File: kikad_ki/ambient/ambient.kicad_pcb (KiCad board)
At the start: 2 copper layers, 80 x 66 mm, 69 parts, among them J1 5V DC, J2 FPC 01x10 Female, J3 LED Array, Q1 2N3904, SW1 Reset, SW2 Next, SW3 Select, SW4 Modify, U1 ATmega328P-PU, U2 AT24C256, U3 AT24C256, U4 AT24C256, U5 AT24C256, Y1 16 MHz

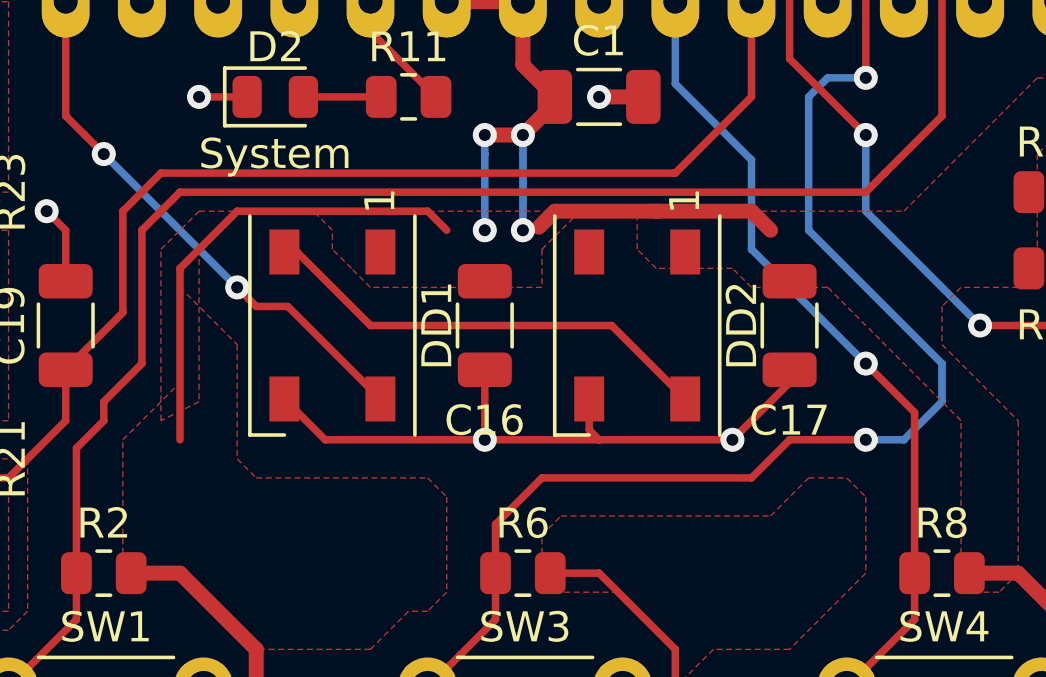
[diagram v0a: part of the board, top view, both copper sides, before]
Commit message: RGB WS2812B -> RGBWW SK6812
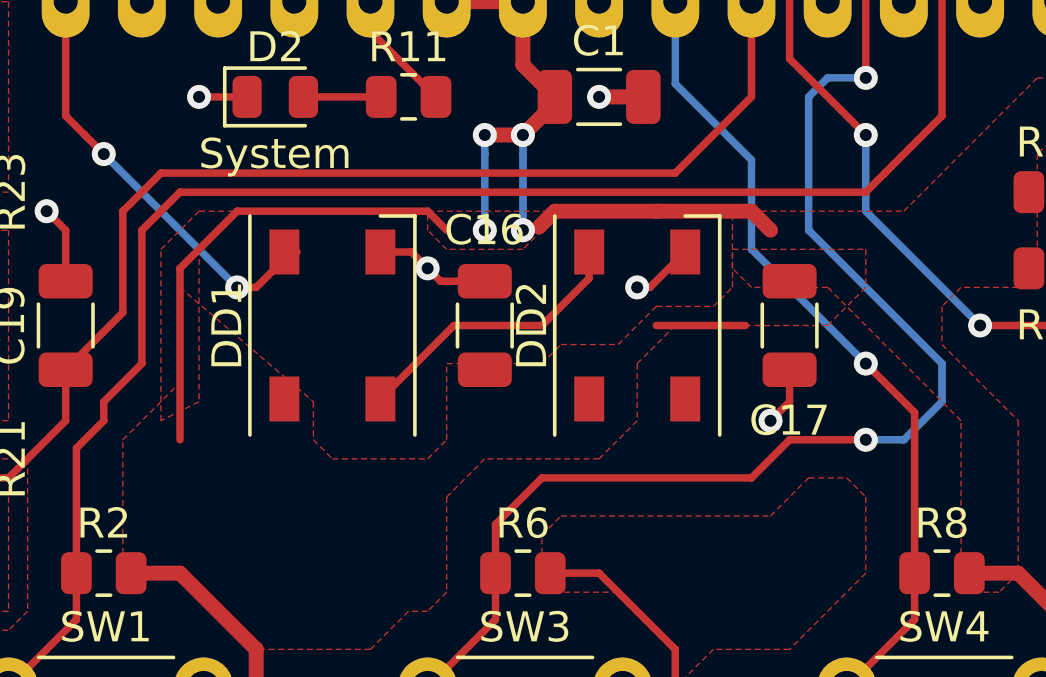
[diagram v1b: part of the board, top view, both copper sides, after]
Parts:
- DD1, DD2: value WS2812B -> SK6812; footprint LED_SMD:LED_WS2812B_PLCC4_5.0x5.0mm_P3.2mm -> LED_SMD:LED_SK6812_PLCC4_5.0x5.0mm_P3.2mm
- turned C16 to 90 degrees
- turned DD1 to 90 degrees
- turned DD2 to 90 degrees
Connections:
- DD1 pad 1: VCC -> GND
- DD1 pad 2: Net-(DD1-Pad2) -> PREVIEW_ARRAY
- DD1 pad 3: GND -> VCC
- DD1 pad 4: PREVIEW_ARRAY -> Net-(DD1-Pad4)
- DD2 pad 1: VCC -> GND
- DD2 pad 2: Net-(DD2-Pad2) -> Net-(DD1-Pad4)
- DD2 pad 3: GND -> VCC
- DD2 pad 4: Net-(DD1-Pad2) -> Net-(DD2-Pad4)
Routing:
- net Net-(DD1-Pad2): track 15.6 -> 0.00 mm
- net GND: track 64.6 -> 50.7 mm, vias 78 -> 79
- net Net-(DD1-Pad4): track 0.00 -> 9.18 mm
- net PREVIEW_ARRAY: track 18.3 -> 14.6 mm
- net VCC: track 165.5 -> 168.5 mm

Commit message: gerber files
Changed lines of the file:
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@@
       (effects (font (size 0.8 0.8) (thickness 0.12)))
     )
-    (pad 1 smd roundrect (at -1.4625 0 90) (size 1.125 1.75) (layers F.Cu F.Paste F.Mask) (roundrect_rratio 0.2222204444444444)
+    (pad 1 smd roundrect (at -1.4625 0 90) (size 1.125 1.75) (layers F.Cu F.Paste F.Mask) (roundrect_rratio 0.2222195555555556)
       (net 2 GND))
-    (pad 2 smd roundrect (at 1.4625 0 90) (size 1.125 1.75) (layers F.Cu F.Paste F.Mask) (roundrect_rratio 0.2222204444444444)
+    (pad 2 smd roundrect (at 1.4625 0 90) (size 1.125 1.75) (layers F.Cu F.Paste F.Mask) (roundrect_rratio 0.2222195555555556)
       (net 37 ARRAY_DIN))
     (model ${KISYS3DMOD}/Resistor_SMD.3dshapes/R_1206_3216Metric.wrl
@@
     (polygon
       (pts
-        (xy 93.98 80.01) (xy 52.07 80.01) (xy 50.165 78.105) (xy 57.15 78.105) (xy 64.135 78.105)
-        (xy 66.675 78.105) (xy 90.17 78.105) (xy 92.075 76.2) (xy 92.075 67.945) (xy 91.44 67.31)
-        (xy 91.44 66.675) (xy 93.98 64.135)
-      )
-    )
+        (xy 93.98 80.01) (xy 52.07 80.01) (xy 50.165 78.105) (xy 57.15 78.105) (xy 61.595 78.105)
+        (xy 64.135 75.565) (xy 66.675 78.105) (xy 90.17 78.105) (xy 92.075 76.2) (xy 92.075 67.945)
+        (xy 91.44 67.31) (xy 91.44 66.675) (xy 93.98 64.135)
+      )
+    )

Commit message: updated design + pcb
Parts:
- removed  : MountingHole_3.2mm_M3, MountingHole:MountingHole_3.2mm_M3 (x3)
- removed the C13 at (86.4, 28.6)
- removed C14, C15, C16, C17, C19: 0.1u, Capacitor_SMD:C_1206_3216Metric
- removed the C3 at (59.4, 26.7)
- removed D4, D5: 1N4735A, Diode_THT:D_DO-41_SOD81_P10.16mm_Horizontal
- removed DD1, DD2: SK6812, LED_SMD:LED_SK6812_PLCC4_5.0x5.0mm_P3.2mm
- removed R14, R15, R16, R17: 4.7k, Resistor_SMD:R_0805_2012Metric
- removed R22, R23: 0.02, Resistor_SMD:R_2512_6332Metric
- removed R9: 68, Resistor_SMD:R_0805_2012Metric
- removed the SW1 at (41.9, 69.2)
- removed SW4: Modify, Button_Switch_THT:SW_PUSH_6mm
- removed U3, U4, U5: AT24C256, Package_DIP:DIP-8_W7.62mm_LongPads
- added ?: , rasp:prv_small, B.Cu at (17.2, 14.8)
- added C6: 22, Capacitor_SMD:C_0805_2012Metric, F.Cu at (51.1, 9.91)
- added H1: MountingHole, MountingHole:MountingHole_3.2mm_M3_DIN965_Pad, F.Cu at (3.56, 13.2)
- added H2: MountingHole, MountingHole:MountingHole_3.2mm_M3_DIN965_Pad, F.Cu at (32.0, 32.3)
- added H3: MountingHole, MountingHole:MountingHole_3.2mm_M3_DIN965_Pad, F.Cu at (76.2, 3.81)
- added H4: MountingHole, MountingHole:MountingHole_3.2mm_M3_DIN965_Pad, F.Cu at (77.4, 32.5)
- added LED1: Blue LED, LED_THT:LED_D3.0mm_Clear, F.Cu at (86.3, 27.8)
- added LED2: Green LED, LED_THT:LED_D3.0mm_Clear, F.Cu at (83.8, 33.4)
- C1: renamed from C6; value 330u 16V -> 100u 25V
- C10: footprint Capacitor_SMD:C_1206_3216Metric -> Capacitor_SMD:C_0805_2012Metric
- C11: renamed from C7; footprint Capacitor_SMD:C_1206_3216Metric -> Capacitor_SMD:C_0805_2012Metric
- C12: renamed from C8; footprint Capacitor_SMD:C_1206_3216Metric -> Capacitor_SMD:C_0805_2012Metric
- C13: renamed from C9; footprint Capacitor_SMD:C_1206_3216Metric -> Capacitor_SMD:C_0805_2012Metric
- C2: renamed from C5; value 330u 16V -> 100u 25V
- C3: renamed from C18; footprint Capacitor_SMD:C_1206_3216Metric -> Capacitor_SMD:C_0805_2012Metric
- C4: renamed from C11; footprint Capacitor_SMD:C_1206_3216Metric -> Capacitor_SMD:C_0805_2012Metric
- C7: renamed from C2; footprint Capacitor_SMD:C_1206_3216Metric -> Capacitor_SMD:C_0805_2012Metric
- C8: renamed from C1; footprint Capacitor_SMD:C_1206_3216Metric -> Capacitor_SMD:C_0805_2012Metric
- C9: renamed from C12; footprint Capacitor_SMD:C_1206_3216Metric -> Capacitor_SMD:C_0805_2012Metric
- D1: value Green LED -> 1N4735A; footprint LED_SMD:LED_0805_2012Metric -> Diode_SMD:D_MiniMELF
- D2: value Blue LED -> 1N4735A; footprint LED_SMD:LED_0805_2012Metric -> Diode_SMD:D_MiniMELF
- D3: footprint Diode_THT:D_DO-41_SOD81_P10.16mm_Horizontal -> Diode_SMD:D_MiniMELF
- J2: value FPC 01x10 Female -> Display; footprint Connector_FFC-FPC:TE_1-84952-0_1x10-1MP_P1.0mm_Horizontal -> Connector_PinHeader_2.54mm:PinHeader_1x09_P2.54mm_Vertical
- L1: value 100u -> 47u
- Q1: value 2N3904 -> MMBT3904; footprint Package_TO_SOT_THT:TO-92 -> Package_TO_SOT_SMD:SOT-23
- R10: value 3k -> 2k
- R11: value 3k -> 1k
- R2: value 5.1k -> 10k
- R3: value 68 -> 100; footprint Resistor_SMD:R_0805_2012Metric -> Resistor_SMD:R_1206_3216Metric
- R5, R7: value 68 -> 200
- R8: value 5.1k -> 100k
- REF**: moved to B.Cu
- moved R5 73.3 mm to (87.4, 3.56), turned to -90 degrees
- moved R3 71.5 mm to (33.5, 6.25), turned to -90 degrees
- moved REF** 70.0 mm to (35.8, 6.84), turned to 180 degrees
- moved C12 68.4 mm to (84.6, 3.56), turned to 90 degrees
- moved C11 63.4 mm to (74.1, 19.6), turned to 0 degrees
- moved R4 62.0 mm to (81.8, 3.66), turned to 90 degrees
- moved SW1 61.9 mm to (81.8, 7.34)
- moved R7 60.3 mm to (87.1, 23.5), turned to 90 degrees
- moved R10 60.3 mm to (88.8, 32.4)
- moved SW2 59.2 mm to (88.3, 19.7), turned to 180 degrees
- moved C13 58.1 mm to (84.3, 23.4)
- moved D2 54.3 mm to (5.34, 19.8), turned to -90 degrees
- moved R2 52.3 mm to (74.1, 21.8)
- moved J3 49.5 mm to (9.00, 18.4)
- moved R6 47.7 mm to (81.8, 23.5), turned to -90 degrees
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- renumbered C4 to C5, SW2 to SW1, SW3 to SW2
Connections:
- C10 pad 1: MODIFY -> AMP_IN
- C12 pad 1: NEXT -> MODE
- D1 pad 1: GND -> +5V
- D1 pad 2: Net-(D1-Pad2) -> GND
- D2 pad 1: GND -> ARRAY_DIN
- D2 pad 2: Net-(D2-Pad2) -> GND
- D3 pad 1: ARRAY_DIN -> ARRAY_GND
- J2 pad 1: LCD_DB7 -> GND
- J2 pad 2: LCD_DB6 -> Net-(J2-Pin_2)
- J2 pad 3: LCD_DB5 -> Net-(J2-Pin_3)
- J2 pad 4: LCD_DB4 -> LCD_RS
- J2 pad 6: LCD_RS -> LCD_DB4
- J2 pad 7: Net-(J2-Pad7) -> LCD_DB5
- J2 pad 8: VCC -> LCD_DB6
- J2 pad 9: GND -> LCD_DB7
- J3 pad 3: AMP_IN -> ARRAY_GND
- Q1 pad 1: ARRAY_DIN -> Net-(Q1-B)
- Q1 pad 2: Net-(Q1-Pad2) -> ARRAY_DIN
- R10 pad 1: Net-(D1-Pad2) -> Net-(LED2-A)
- R11 pad 1: Net-(D2-Pad2) -> Net-(LED1-A)
- R18 pad 2: Net-(Q1-Pad2) -> Net-(Q1-B)
- R20 pad 2: AMP_IN -> ARRAY_GND
- R21 pad 1: Net-(R20-Pad1) -> GND
- R21 pad 2: AMP_IN -> Net-(R20-Pad1)
- R3 pad 1: GND -> Net-(J2-Pin_2)
- R3 pad 2: Net-(R3-Pad2) -> VCC
- R4 pad 1: NEXT -> MODE
- R8 pad 1: MODIFY -> ARRAY_GND
- R8 pad 2: VCC -> AMP_IN
- RV1 pad 2: Net-(J2-Pad7) -> Net-(J2-Pin_3)
- SW1 pad 1: NEXT -> MODE
- U1 pad 15: PREVIEW_ARRAY -> unconnected-(U1-PB1-Pad15)
- U1 pad 18: Net-(U1-Pad18) -> unconnected-(U1-PB4-Pad18)
- U1 pad 2: Net-(U1-Pad2) -> unconnected-(U1-PD0-Pad2)
- U1 pad 23: MODIFY -> unconnected-(U1-PC0-Pad23)
- U1 pad 25: Net-(U1-Pad25) -> SELECT
- U1 pad 26: Net-(U1-Pad26) -> MODE
- U1 pad 3: Net-(U1-Pad3) -> unconnected-(U1-PD1-Pad3)
- U1 pad 4: SELECT -> unconnected-(U1-PD2-Pad4)
- U1 pad 5: NEXT -> unconnected-(U1-PD3-Pad5)
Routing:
- net VCC: track 168.5 -> 13.3 mm, vias 6 -> 12
- net RESET: track 69.3 -> 5.32 mm
- net AMP_IN: track 69.0 -> 5.40 mm
- net SCL: track 80.6 -> 17.9 mm, vias 6 -> 0
- net SDA: track 79.5 -> 17.5 mm
- net ARRAY_GND: track 0.00 -> 60.1 mm, vias 0 -> 2
- net MODE: track 0.00 -> 53.7 mm, vias 0 -> 4
- net NEXT: track 52.8 -> 0.00 mm, vias 2 -> 0
- net MODIFY: track 37.9 -> 0.00 mm, vias 1 -> 0
- net LED: track 4.08 -> 33.4 mm, vias 0 -> 1
- net SELECT: track 58.6 -> 36.4 mm
- net ARRAY_DIN: track 45.2 -> 26.3 mm
- net Net-(J2-Pin_3): track 0.00 -> 15.8 mm
- net PREVIEW_ARRAY: track 14.2 -> 0.00 mm, vias 2 -> 0
- net GND: track 50.7 -> 39.2 mm, vias 79 -> 27
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- added copper zone on B.Cu, net VCC
- removed copper zone on B.Cu, net +5V
- removed copper zone on F.Cu, net AMP_IN
- removed copper zone on F.Cu, net Net-(R20-Pad1)
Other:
- board size 80 x 66 mm -> 90 x 36 mm
- net class Default removed
- board text added: "JLCJLCJLCJLC"
- board text removed: "Power"
- board text removed: "System"
